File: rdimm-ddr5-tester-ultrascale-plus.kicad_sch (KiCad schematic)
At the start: 2 parts

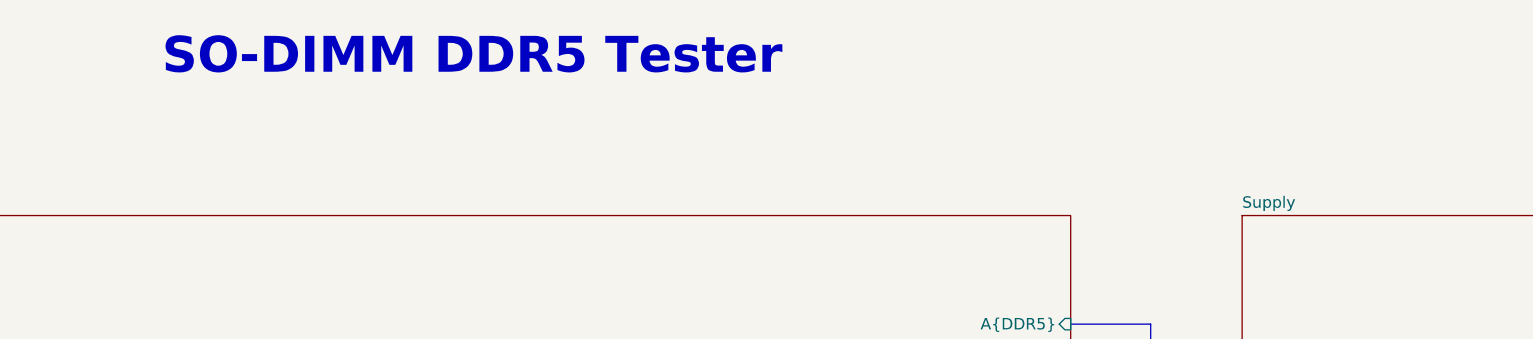
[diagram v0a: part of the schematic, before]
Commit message: [#65754] Update PCB outline and rename the board
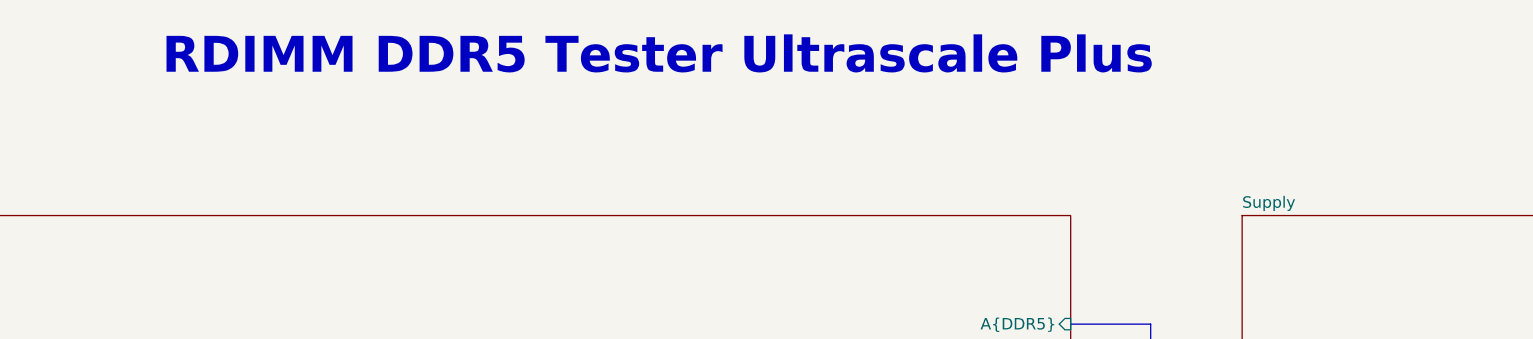
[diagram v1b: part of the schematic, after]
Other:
- note added: "RDIMM DDR5 Tester Ultrascale Plus"
- note removed: "SO-DIMM DDR5 Tester"
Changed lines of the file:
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@@
     (effects (font (size 1.27 1.27)) (justify left bottom))
   )
-  (text "SO-DIMM DDR5 Tester" (at 172.085 35.56 0)
+  (text "RDIMM DDR5 Tester Ultrascale Plus" (at 172.085 35.56 0)
     (effects (font (size 3.9878 3.9878) (thickness 0.7976) bold) (justify left bottom))
   )

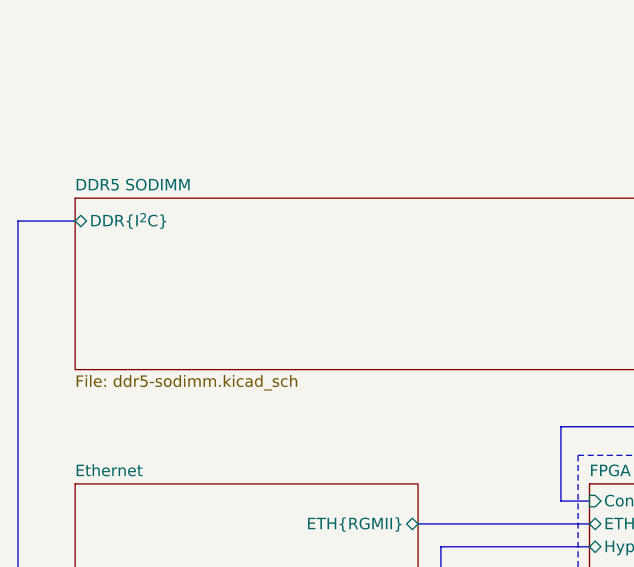
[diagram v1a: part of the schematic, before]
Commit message: [#65754] Replace so-dimm with rdimm connector
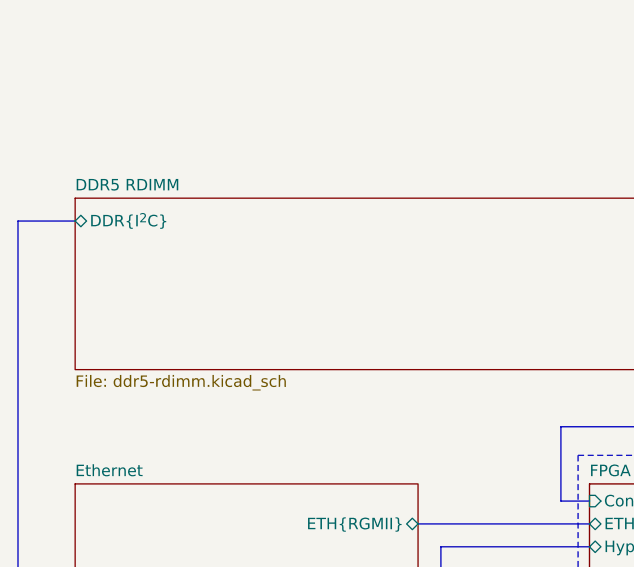
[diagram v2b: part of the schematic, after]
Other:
- sheet DDR5 SODIMM renamed DDR5 RDIMM
- sheet DDR5 RDIMM: file ddr5-sodimm.kicad_sch -> ddr5-rdimm.kicad_sch
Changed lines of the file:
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@@
     (stroke (width 0) (type solid))
     (fill (color 0 0 0 0.0000))
-    (property "Sheetname" "DDR5 SODIMM" (at 88.9 50.0884 0)
+    (property "Sheetname" "DDR5 RDIMM" (at 88.9 50.0884 0)
       (effects (font (size 1.27 1.27)) (justify left bottom))
     )
-    (property "Sheetfile" "ddr5-sodimm.kicad_sch" (at 88.9 70.4346 0)
+    (property "Sheetfile" "ddr5-rdimm.kicad_sch" (at 88.9 70.4346 0)
       (effects (font (size 1.27 1.27)) (justify left top))
     )
